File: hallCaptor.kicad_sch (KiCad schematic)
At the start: 1 part, among them U6 Hall Sensor A3144

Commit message: add: bom
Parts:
- U6: Price (none) -> 1.12; SUPPLIER (none) -> https://www.lcsc.com/product-detail/C18221460.html
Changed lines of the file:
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@@
+			)
+		)
+		(property "Minimum quantity per command" ""
+			(at 66.04 38.1 0)
+			(hide yes)
+			(show_name no)
+			(do_not_autoplace no)
+			(effects
+				(font
+					(size 1.27 1.27)
+				)
+			)
+		)
+		(property "Price" "1.12"
+			(at 66.04 38.1 0)
+			(hide yes)
+			(show_name no)
+			(do_not_autoplace no)
+			(effects
+				(font
+					(size 1.27 1.27)
+				)
+			)
+		)
+		(property "SUPPLIER" "https://www.lcsc.com/product-detail/C18221460.html"
+			(at 66.04 38.1 0)
+			(hide yes)
+			(show_name no)
+			(do_not_autoplace no)
+			(effects
+				(font
+					(size 1.27 1.27)
+				)
 			)
 		)
@@
 			(at 66.04 50.8 0)
 			(hide yes)
+			(show_name no)
+			(do_not_autoplace no)
+			(effects
+				(font
+					(size 1.27 1.27)
+				)
+			)
+		)
+		(property "Minimum quantity per command" ""
+			(at 66.04 50.8 0)
+			(hide yes)

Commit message: finished all footprints + redid some symbols, ready for PCB
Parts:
- U6: footprint (none) -> G-Love:Hall_Sensor_A3144
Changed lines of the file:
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@@
 			)
 		)
-		(property "Footprint" ""
+		(property "Footprint" "G-Love:Hall_Sensor_A3144"
 			(at 66.04 38.1 0)
 			(hide yes)

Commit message: update: footprint link to component
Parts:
- U6: footprint G-Love:Hall_Sensor_A3144 -> MyGlove:Hall_Sensor_A3144
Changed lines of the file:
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@@
 			)
 		)
-		(property "Footprint" "G-Love:Hall_Sensor_A3144"
+		(property "Footprint" "MyGlove:Hall_Sensor_A3144"
 			(at 66.04 38.1 0)
 			(hide yes)

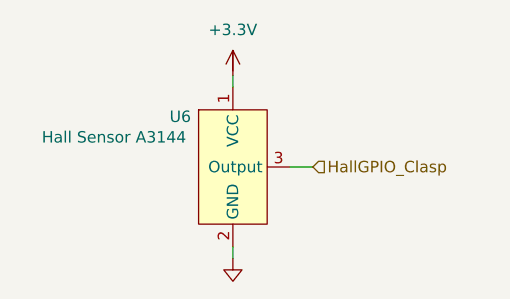
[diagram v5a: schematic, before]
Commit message: routing: functional blocks
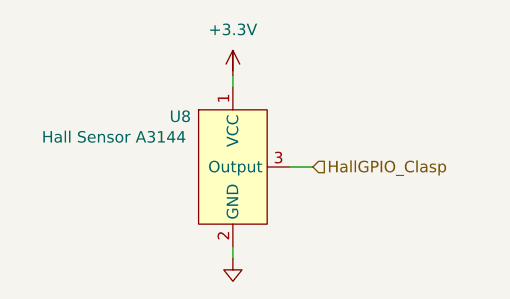
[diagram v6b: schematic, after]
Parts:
- renumbered U6 to U8
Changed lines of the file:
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@@
 		(in_pos_files yes)
 		(dnp no)
-		(property "Reference" "U6"
+		(property "Reference" "U8"
 			(at 60.198 35.052 0)
 			(show_name no)
@@
 			(project "G-Love"
 				(path "/808bc5ea-49ac-4454-ba77-8b20d01ce159/c9027db4-6968-4e40-a138-b60eacbff4db/52001651-8f72-422f-9b98-937203a79121"
-					(reference "U6")
+					(reference "U8")
 					(unit 1)
 				)
@@
 		(in_pos_files yes)
 		(dnp no)
-		(property "Reference" "GND027"
+		(property "Reference" "GND034"
 			(at 66.04 54.356 0)
 			(hide yes)
@@
 			(project "G-Love"
 				(path "/808bc5ea-49ac-4454-ba77-8b20d01ce159/c9027db4-6968-4e40-a138-b60eacbff4db/52001651-8f72-422f-9b98-937203a79121"
-					(reference "GND027")
+					(reference "GND034")
 					(unit 1)
 				)
@@
 		(dnp no)
 		(fields_autoplaced yes)
-		(property "Reference" "#PWR022"
+		(property "Reference" "#PWR030"
 			(at 69.85 30.988 0)
 			(hide yes)
@@
 			(project "G-Love"
 				(path "/808bc5ea-49ac-4454-ba77-8b20d01ce159/c9027db4-6968-4e40-a138-b60eacbff4db/52001651-8f72-422f-9b98-937203a79121"
-					(reference "#PWR022")
+					(reference "#PWR030")
 					(unit 1)
 				)
